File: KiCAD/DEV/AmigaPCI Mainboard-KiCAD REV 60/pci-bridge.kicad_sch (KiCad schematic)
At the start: 46 parts, among them CN109 SPI, CN110 SPI, U109 ICE40HX4K-TQ144, U109F1 W25X20CLSN, U110 ICE40HX4K-TQ144, U110F1 W25X20CLSN

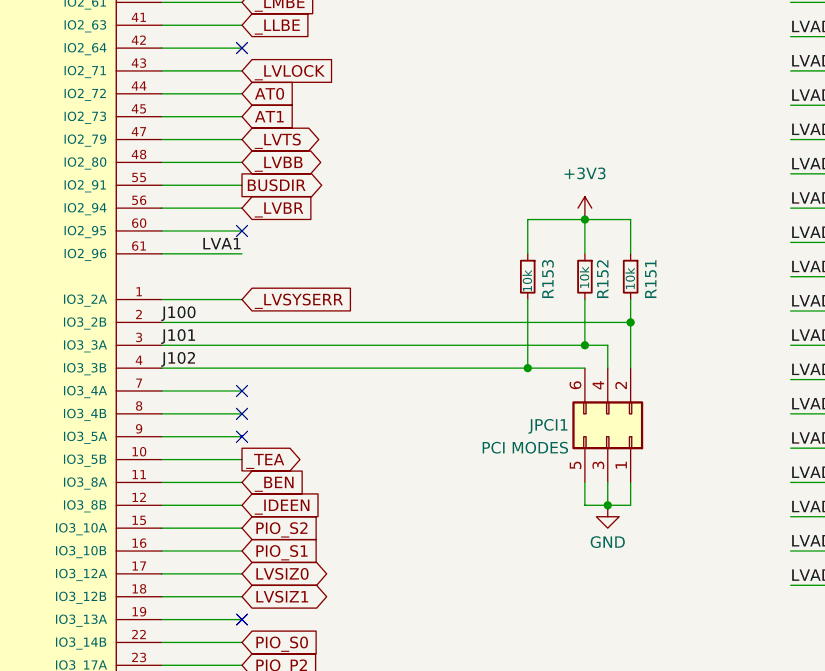
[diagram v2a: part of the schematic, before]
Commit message: APCI Rev 6.0 Work
Add ROM wait state jumpers.
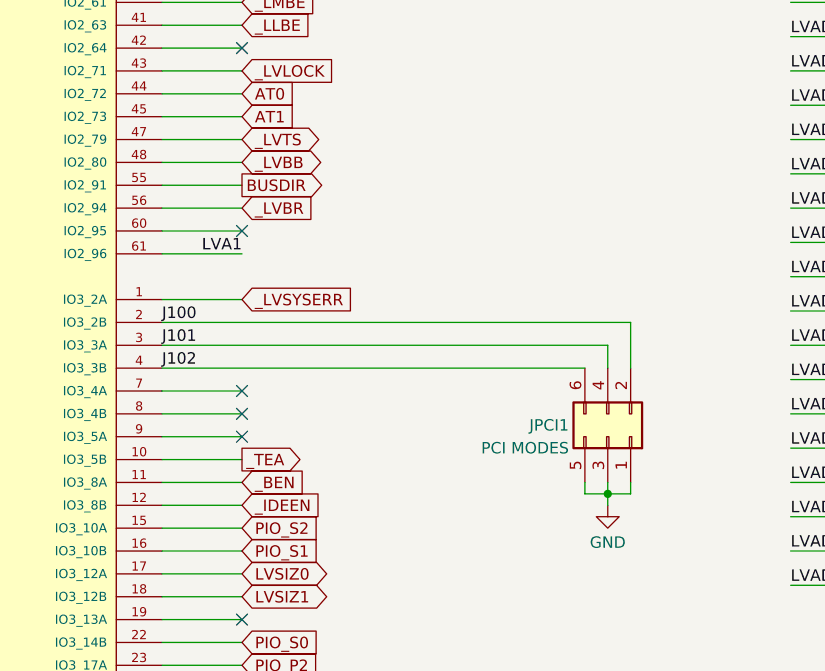
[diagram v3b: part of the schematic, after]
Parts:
- removed R151, R152, R153: 10k, Resistor_SMD:R_0603_1608Metric, symbol Device:R_Small

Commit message: APCI Rev 6.0 work.
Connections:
- net AT0 renamed PCIAT0
- net AT1 renamed PCIAT1
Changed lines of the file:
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@@
 	(title_block
 		(title "AMIGA PCI")
-		(date "2025-05-24")
+		(date "2025-05-27")
 		(rev "6.0")
 	)
@@
 		)
 	)
-	(global_label "AT0"
+	(global_label "PCIAT0"
 		(shape input)
 		(at 281.94 129.54 0)
@@
 		)
 		(property "Intersheetrefs" "${INTERSHEET_REFS}"
-			(at 288.1909 129.54 0)
+			(at 291.3357 129.54 0)
 			(effects
 				(font
@@
 		)
 	)
-	(global_label "AT1"
+	(global_label "PCIAT1"
 		(shape input)
 		(at 281.94 132.08 0)
@@
 		)
 		(property "Intersheetrefs" "${INTERSHEET_REFS}"
-			(at 288.1909 132.08 0)
+			(at 291.3357 132.08 0)
 			(effects
 				(font

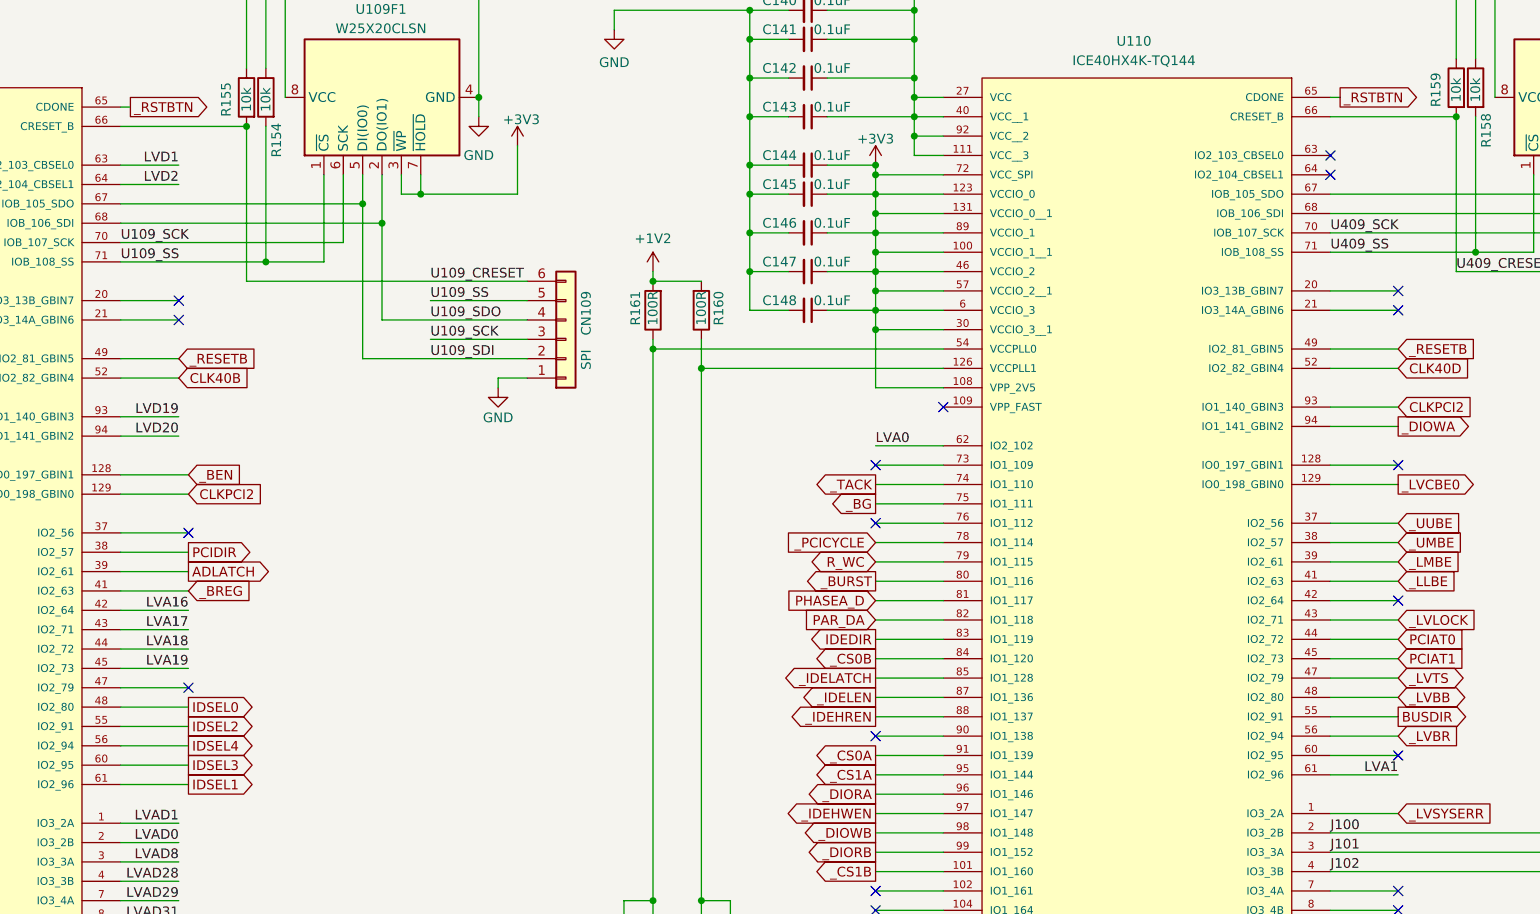
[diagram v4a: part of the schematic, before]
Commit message: Rev 6.0 APCI Work
Added ATA address lines to U110.
Cleaned up some routing.
Removed address lines from U109 - we can pick them up from the AD bus.
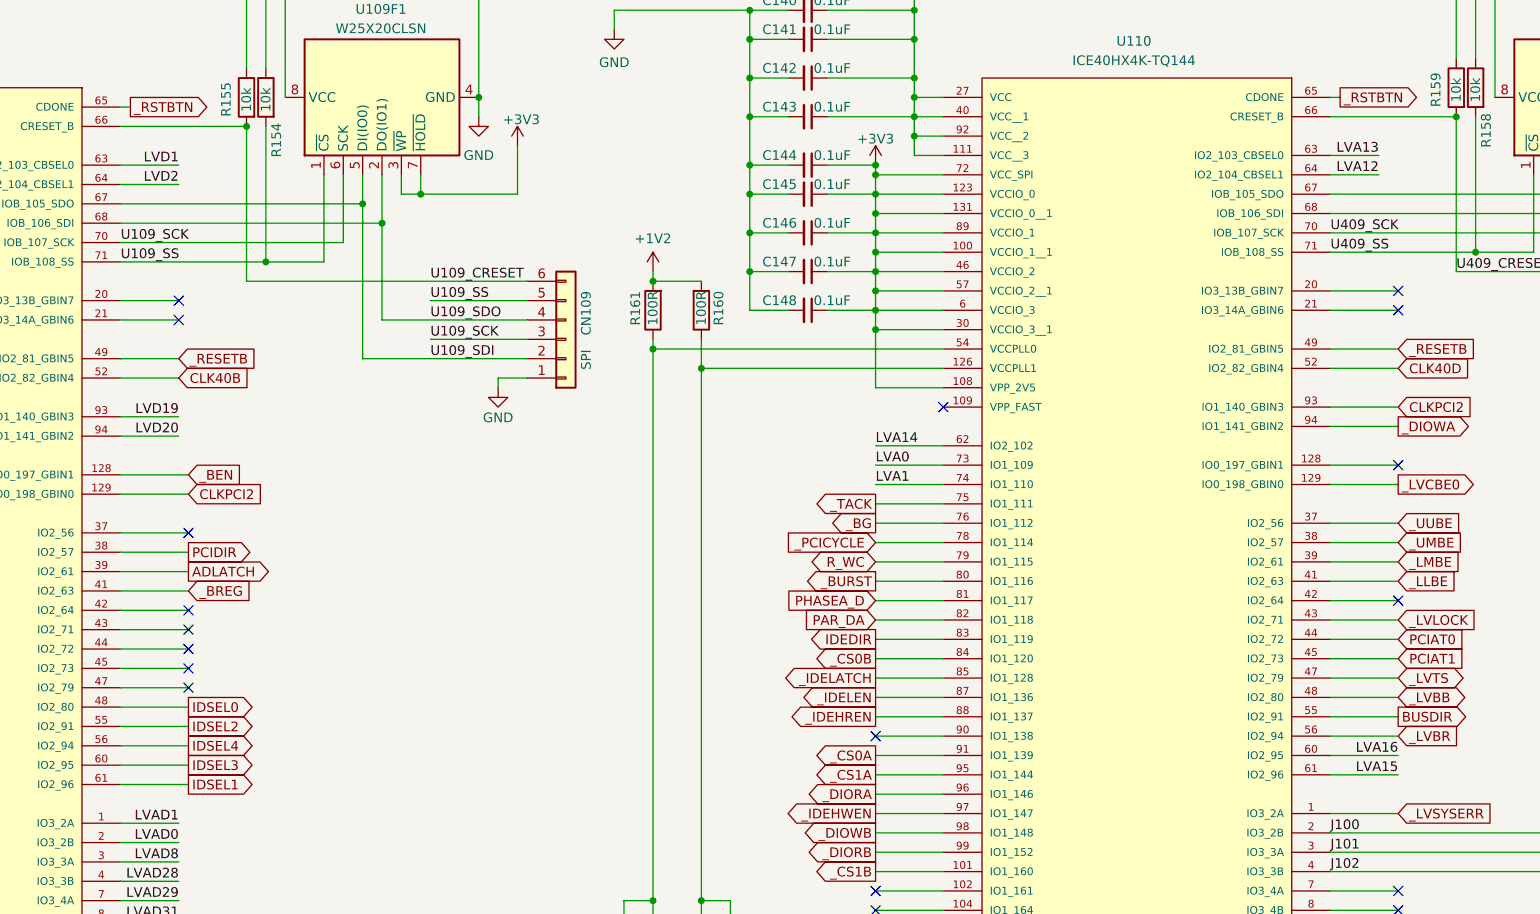
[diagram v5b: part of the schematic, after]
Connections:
- net LVA0: now also U110.73 (IO1_109); no longer U110.62 (IO2_102)
- net LVA1: now also U110.74 (IO1_110); no longer U110.61 (IO2_96)
- net LVA12: now also U110.64 (IO2_104_CBSEL1)
- net LVA13: now also U110.63 (IO2_103_CBSEL0)
- net LVA14: now also U110.62 (IO2_102)
- net LVA15: now also U110.61 (IO2_96)
- net LVA16: now also U110.60 (IO2_95); no longer U109.42 (IO2_64)
- net LVA17: no longer U109.43 (IO2_71)
- net LVA18: no longer U109.44 (IO2_72)
- net LVA19: no longer U109.45 (IO2_73)
- net _BG: now also U110.76 (IO1_112); no longer U110.75 (IO1_111)
- net _TACK: now also U110.75 (IO1_111); no longer U110.74 (IO1_110)
- no-connect marks 39 -> 38
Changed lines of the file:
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@@
 	)
 	(no_connect
-		(at 281.94 210.82)
+		(at 123.19 128.27)
 	)
 	(no_connect
-		(at 213.36 106.68)
+		(at 121.92 214.63)
 	)
 	(no_connect
-		(at 121.92 214.63)
+		(at 123.19 135.89)
+	)
+	(no_connect
+		(at 123.19 125.73)
 	)
 	(no_connect
@@
 	)
 	(no_connect
-		(at 281.94 213.36)
-	)
-	(no_connect
 		(at 121.92 201.93)
 	)
@@
 	)
 	(no_connect
-		(at 281.94 208.28)
+		(at 281.94 200.66)
 	)
 	(no_connect
-		(at 281.94 144.78)
+		(at 281.94 210.82)
 	)
 	(no_connect
@@
 	)
 	(no_connect
-		(at 123.19 135.89)
-	)
-	(no_connect
-		(at 273.05 66.04)
+		(at 281.94 203.2)
 	)
 	(no_connect
-		(at 213.36 114.3)
+		(at 281.94 208.28)
 	)
 	(no_connect
-		(at 281.94 205.74)
+		(at 281.94 106.68)
 	)
 	(no_connect
-		(at 281.94 106.68)
+		(at 123.19 115.57)
 	)
 	(no_connect
-		(at 273.05 68.58)
+		(at 281.94 205.74)
 	)
 	(no_connect
@@
 	)
 	(no_connect
-		(at 281.94 215.9)
-	)
-	(no_connect
 		(at 213.36 165.1)
 	)
@@
 	)
 	(no_connect
-		(at 281.94 200.66)
-	)
-	(no_connect
 		(at 121.92 209.55)
 	)
@@
 	)
 	(no_connect
+		(at 281.94 215.9)
+	)
+	(no_connect
+		(at 123.19 133.35)
+	)
+	(no_connect
 		(at 121.92 212.09)
 	)
 	(no_connect
-		(at 222.25 99.06)
+		(at 123.19 130.81)
 	)
 	(no_connect
-		(at 123.19 115.57)
+		(at 222.25 99.06)
 	)
 	(no_connect
@@
 	)
 	(no_connect
-		(at 281.94 124.46)
+		(at 281.94 213.36)
 	)
 	(no_connect
-		(at 121.92 85.09)
+		(at 281.94 124.46)
 	)
 	(no_connect
-		(at 281.94 203.2)
+		(at 121.92 85.09)
 	)
 	(no_connect
@@
 	(wire
 		(pts
+			(xy 279.4 66.04) (xy 273.05 66.04)
+		)
+		(stroke
+			(width 0)
+			(type default)
+		)
+	)
+	(wire
+		(pts
 			(xy 143.51 77.47) (xy 114.3 77.47)
 		)
@@
 	(wire
 		(pts
+			(xy 279.4 68.58) (xy 273.05 68.58)
+		)
+		(stroke
+			(width 0)
+			(type default)
+		)
+	)
+	(wire
+		(pts
 			(xy 63.5 85.09) (xy 53.34 85.09)
 		)
@@
 		)
 	)
+	(label "LVA12"
+		(at 279.4 68.58 180)
+		(effects
+			(font
+				(size 1.27 1.27)
+			)
+			(justify right bottom)
+		)
+	)
 	(label "LVD25"
 		(at 383.54 175.26 0)
@@
 		)
 	)
+	(label "LVA15"
+		(at 281.94 147.32 180)
+		(effects
+			(font
+				(size 1.27 1.27)
+			)
+			(justify right bottom)
+		)
+	)
 	(label "LVAD6"
 		(at 342.9 88.9 0)
@@
 	)
 	(label "LVA0"
-		(at 213.36 104.14 0)
+		(at 213.36 106.68 0)
 		(effects
 			(font
@@
 		)
 	)
-	(label "LVA19"
-		(at 123.19 133.35 180)
-		(effects
-			(font
-				(size 1.27 1.27)
-			)
-			(justify right bottom)
-		)
-	)
-	(label "LVA18"
-		(at 123.19 130.81 180)
-		(effects
-			(font
-				(size 1.27 1.27)
-			)
-			(justify right bottom)
-		)
-	)
 	(label "U109_SS"
 		(at 114.3 80.01 0)
@@
 		)
 	)
+	(label "LVA14"
+		(at 213.36 104.14 0)
+		(effects
+			(font
+				(size 1.27 1.27)
+			)
+			(justify left bottom)
+		)
+	)
 	(label "LVA26"
 		(at 363.22 170.18 0)
@@
 		)
 	)
-	(label "LVA16"
-		(at 123.19 125.73 180)
-		(effects
-			(font
-				(size 1.27 1.27)
-			)
-			(justify right bottom)
-		)
-	)
 	(label "LVD21"
 		(at 54.61 148.59 0)
@@
 	)
 	(label "LVA1"
-		(at 281.94 147.32 180)
+		(at 213.36 109.22 0)
 		(effects
 			(font
 				(size 1.27 1.27)
 			)
-			(justify right bottom)
+			(justify left bottom)
 		)
 	)
@@
 		)
 	)
+	(label "LVA13"
+		(at 279.4 66.04 180)
+		(effects
+			(font
+				(size 1.27 1.27)
+			)
+			(justify right bottom)
+		)
+	)
 	(label "U409_SDI"
 		(at 314.96 91.44 0)
@@
 		)
 	)
+	(label "LVA16"
+		(at 281.94 144.78 180)
+		(effects
+			(font
+				(size 1.27 1.27)
+			)
+			(justify right bottom)
+		)
+	)
 	(label "LVD27"
 		(at 383.54 182.88 0)
@@
 		)
 	)
-	(label "LVA17"
-		(at 123.19 128.27 180)
-		(effects
-			(font
-				(size 1.27 1.27)
-			)
-			(justify right bottom)
-		)
-	)
 	(label "LVAD22"
 		(at 342.9 149.86 0)
@@
 	(global_label "_BG"
 		(shape output)
-		(at 213.36 111.76 180)
+		(at 213.36 114.3 180)
 		(fields_autoplaced yes)
 		(effects
@@
 		)
 		(property "Intersheetrefs" "${INTERSHEET_REFS}"
-			(at 206.8672 111.76 0)
+			(at 206.8672 114.3 0)
 			(effects
 				(font
@@
 	(global_label "_TACK"
 		(shape output)
-		(at 213.36 109.22 180)
+		(at 213.36 111.76 180)
 		(fields_autoplaced yes)
 		(effects
@@
 		)
 		(property "Intersheetrefs" "${INTERSHEET_REFS}"
-			(at 204.811 109.22 0)
+			(at 204.811 111.76 0)
 			(effects
 				(font
